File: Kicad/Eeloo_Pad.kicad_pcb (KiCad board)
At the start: 2 copper layers, 61 parts, among them IC1 W25Q16JVUXIQ_TR, IC2 W25Q16JVUXIQ_TR, J1 USB_C_Receptacle_USB2.0_16P, J2 Conn_01x13, J3 SC0914_13_, J4 SC0914_13_, SW1 SW_Push, SW2 SW_Push, SW3 SW_Push, SW4 SW_Push, U1 HT16K33A-28SSOP, U2 HT16K33A-28SSOP, U3 HT16K33A-28SSOP, U4 HT16K33A-28SSOP, U5 HT16K33A-28SSOP, U6 HT16K33A-28SSOP, Y1 ABM8-272-T3, Y2 ABM8-272-T3

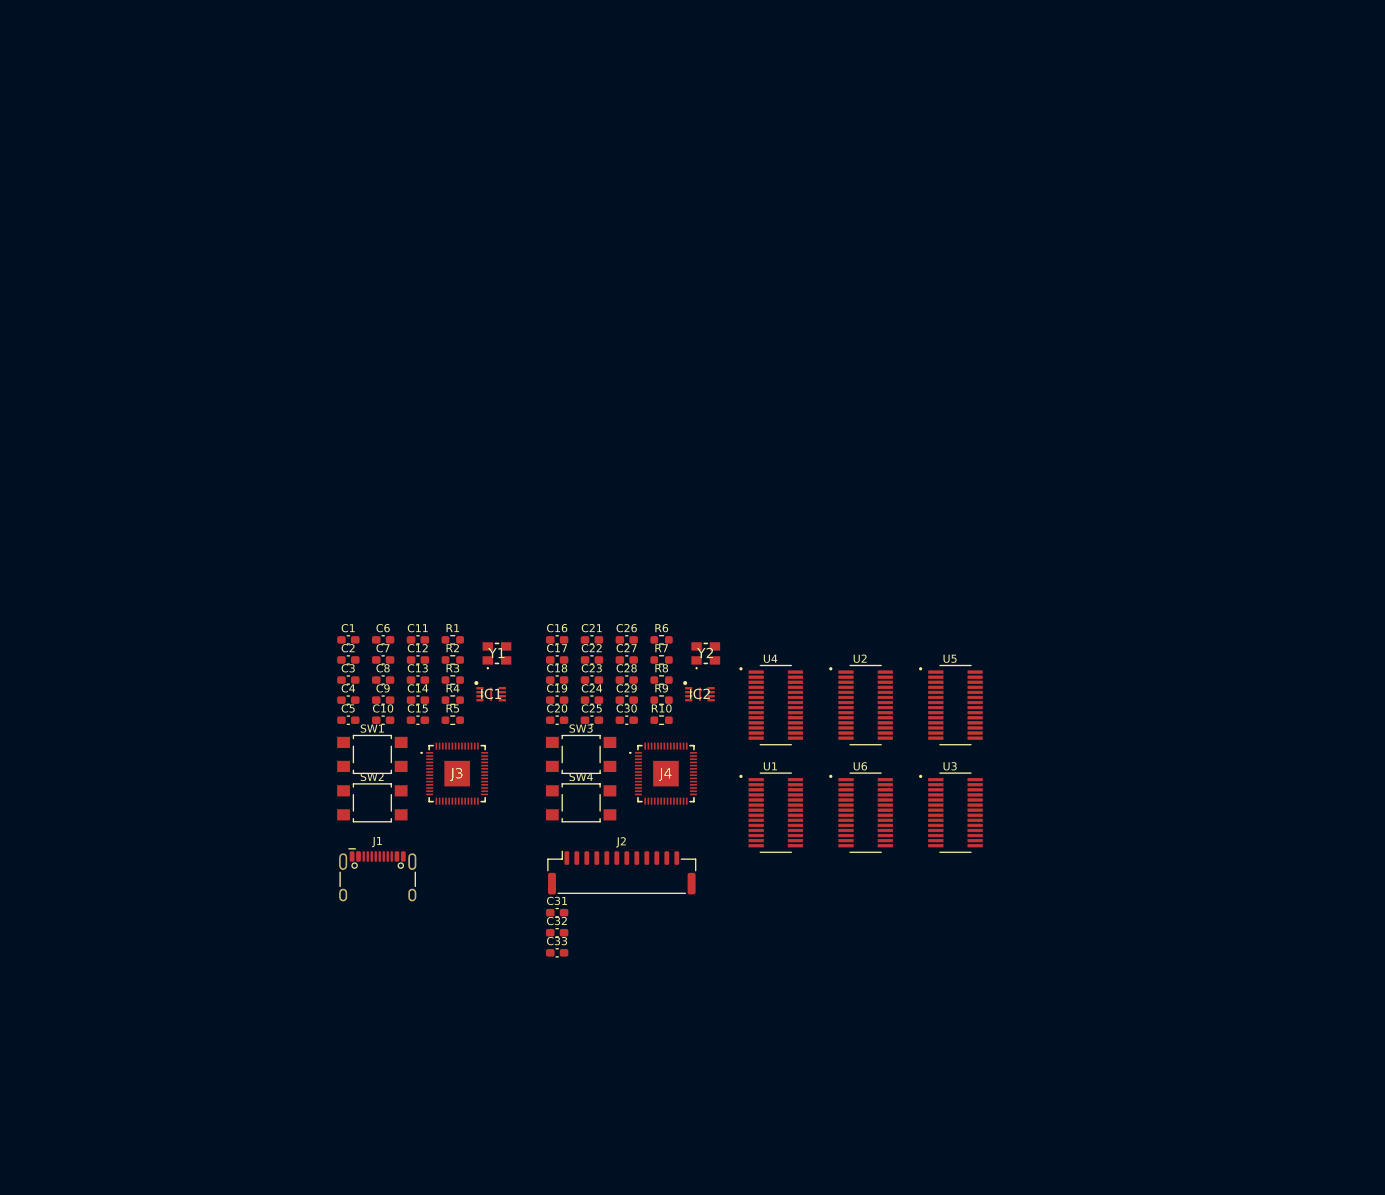
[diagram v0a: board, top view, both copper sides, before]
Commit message: adding multiple component (14 semgent and led)
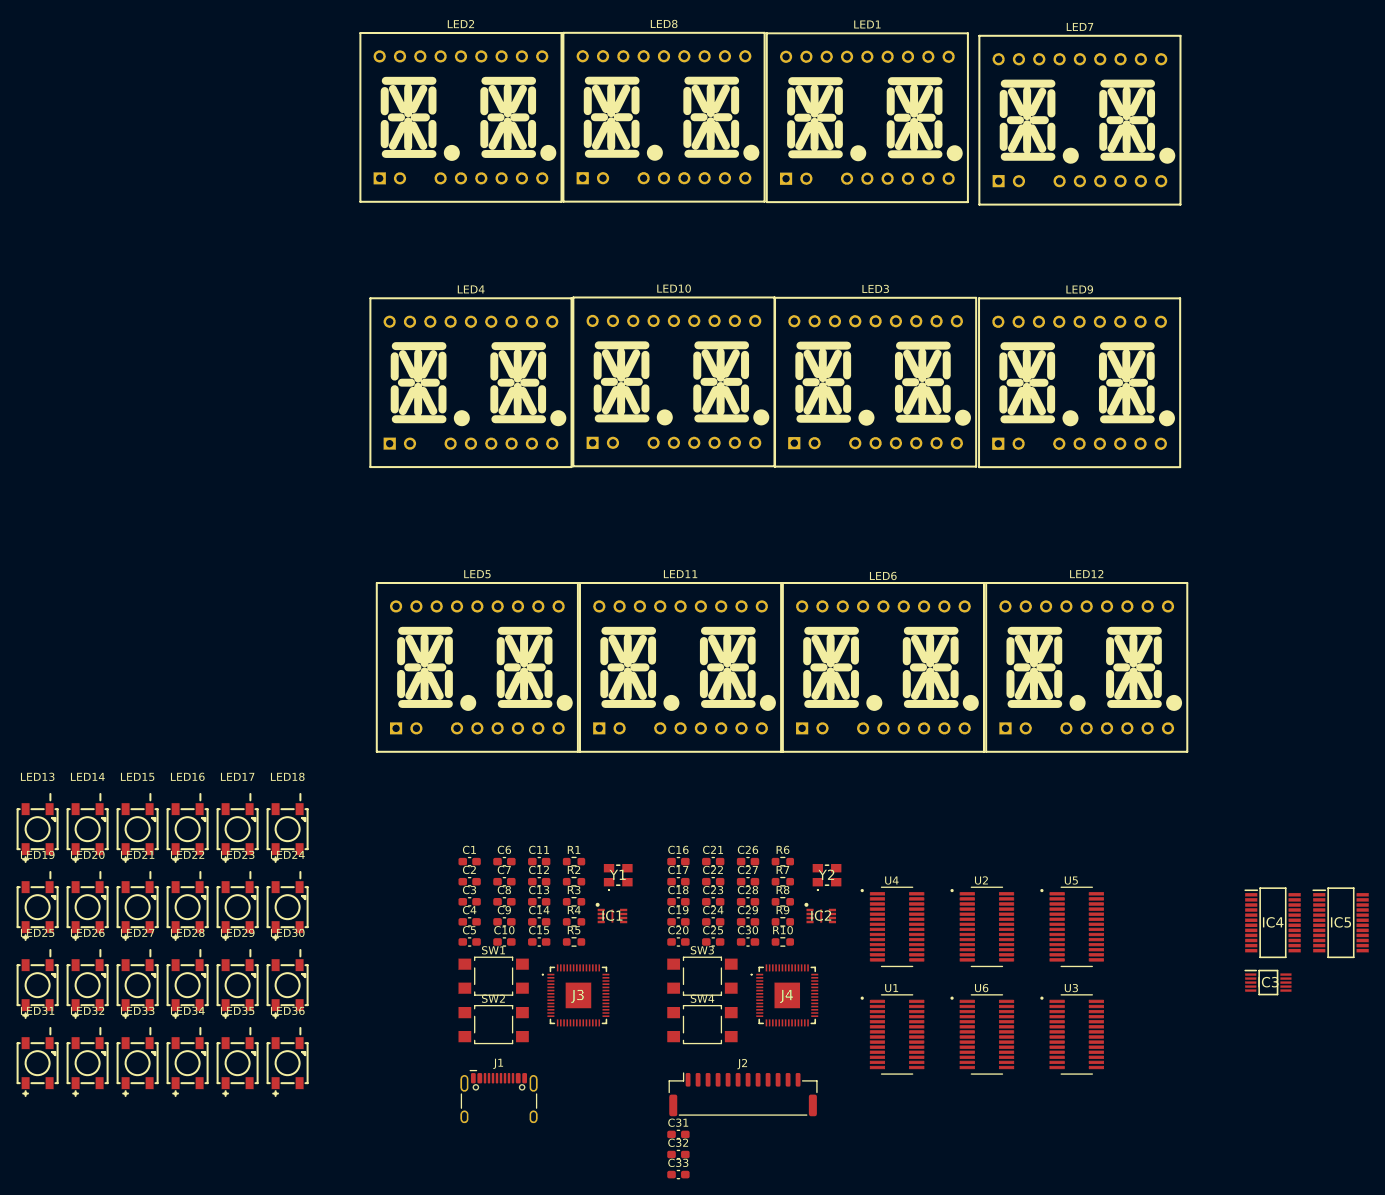
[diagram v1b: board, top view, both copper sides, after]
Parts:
- added IC3: ADS1015IDGST, Eeloo_Pad:SOP50P490X110-10N, F.Cu at (237.6, 138.8)
- added IC4: PCF8575DBQR, Eeloo_Pad:SOP64P600X175-24N, F.Cu at (238.2, 131.3)
- added IC5: PCF8575DBQR, Eeloo_Pad:SOP64P600X175-24N, F.Cu at (246.7, 131.3)
- added LED1: FJ5241AH, Eeloo_Pad:LED-SEG-TH_18P-L25.2-W21.1-P2.54-LS15.2-BL, F.Cu at (187.5, 30.7)
- added LED10: FJ5241AH, Eeloo_Pad:LED-SEG-TH_18P-L25.2-W21.1-P2.54-LS15.2-BL, F.Cu at (163.3, 63.7)
- added LED11: FJ5241AH, Eeloo_Pad:LED-SEG-TH_18P-L25.2-W21.1-P2.54-LS15.2-BL, F.Cu at (164.2, 99.4)
- added LED12: FJ5241AH, Eeloo_Pad:LED-SEG-TH_18P-L25.2-W21.1-P2.54-LS15.2-BL, F.Cu at (214.9, 99.4)
- added LED13: XL-5050RGBC-WS2812B, Eeloo_Pad:LED-SMD_4P-L5.0-W5.0-BL_XL-5050RGBC, F.Cu at (83.8, 119.6)
- added LED14: XL-5050RGBC-WS2812B, Eeloo_Pad:LED-SMD_4P-L5.0-W5.0-BL_XL-5050RGBC, F.Cu at (90.0, 119.6)
- added LED15: XL-5050RGBC-WS2812B, Eeloo_Pad:LED-SMD_4P-L5.0-W5.0-BL_XL-5050RGBC, F.Cu at (96.3, 119.6)
- added LED16: XL-5050RGBC-WS2812B, Eeloo_Pad:LED-SMD_4P-L5.0-W5.0-BL_XL-5050RGBC, F.Cu at (102.5, 119.6)
- added LED17: XL-5050RGBC-WS2812B, Eeloo_Pad:LED-SMD_4P-L5.0-W5.0-BL_XL-5050RGBC, F.Cu at (108.8, 119.6)
- added LED18: XL-5050RGBC-WS2812B, Eeloo_Pad:LED-SMD_4P-L5.0-W5.0-BL_XL-5050RGBC, F.Cu at (115.0, 119.6)
- added LED19: XL-5050RGBC-WS2812B, Eeloo_Pad:LED-SMD_4P-L5.0-W5.0-BL_XL-5050RGBC, F.Cu at (83.8, 129.4)
- added LED2: FJ5241AH, Eeloo_Pad:LED-SEG-TH_18P-L25.2-W21.1-P2.54-LS15.2-BL, F.Cu at (136.7, 30.7)
- added LED20: XL-5050RGBC-WS2812B, Eeloo_Pad:LED-SMD_4P-L5.0-W5.0-BL_XL-5050RGBC, F.Cu at (90.0, 129.4)
- added LED21: XL-5050RGBC-WS2812B, Eeloo_Pad:LED-SMD_4P-L5.0-W5.0-BL_XL-5050RGBC, F.Cu at (96.3, 129.4)
- added LED22: XL-5050RGBC-WS2812B, Eeloo_Pad:LED-SMD_4P-L5.0-W5.0-BL_XL-5050RGBC, F.Cu at (102.5, 129.4)
- added LED23: XL-5050RGBC-WS2812B, Eeloo_Pad:LED-SMD_4P-L5.0-W5.0-BL_XL-5050RGBC, F.Cu at (108.8, 129.4)
- added LED24: XL-5050RGBC-WS2812B, Eeloo_Pad:LED-SMD_4P-L5.0-W5.0-BL_XL-5050RGBC, F.Cu at (115.0, 129.4)
- added LED25: XL-5050RGBC-WS2812B, Eeloo_Pad:LED-SMD_4P-L5.0-W5.0-BL_XL-5050RGBC, F.Cu at (83.8, 139.1)
- added LED26: XL-5050RGBC-WS2812B, Eeloo_Pad:LED-SMD_4P-L5.0-W5.0-BL_XL-5050RGBC, F.Cu at (90.0, 139.1)
- added LED27: XL-5050RGBC-WS2812B, Eeloo_Pad:LED-SMD_4P-L5.0-W5.0-BL_XL-5050RGBC, F.Cu at (96.3, 139.1)
- added LED28: XL-5050RGBC-WS2812B, Eeloo_Pad:LED-SMD_4P-L5.0-W5.0-BL_XL-5050RGBC, F.Cu at (102.5, 139.1)
- added LED29: XL-5050RGBC-WS2812B, Eeloo_Pad:LED-SMD_4P-L5.0-W5.0-BL_XL-5050RGBC, F.Cu at (108.8, 139.1)
- added LED3: FJ5241AH, Eeloo_Pad:LED-SEG-TH_18P-L25.2-W21.1-P2.54-LS15.2-BL, F.Cu at (188.6, 63.8)
- added LED30: XL-5050RGBC-WS2812B, Eeloo_Pad:LED-SMD_4P-L5.0-W5.0-BL_XL-5050RGBC, F.Cu at (115.0, 139.1)
- added LED31: XL-5050RGBC-WS2812B, Eeloo_Pad:LED-SMD_4P-L5.0-W5.0-BL_XL-5050RGBC, F.Cu at (83.8, 148.9)
- added LED32: XL-5050RGBC-WS2812B, Eeloo_Pad:LED-SMD_4P-L5.0-W5.0-BL_XL-5050RGBC, F.Cu at (90.0, 148.9)
- added LED33: XL-5050RGBC-WS2812B, Eeloo_Pad:LED-SMD_4P-L5.0-W5.0-BL_XL-5050RGBC, F.Cu at (96.3, 148.9)
- added LED34: XL-5050RGBC-WS2812B, Eeloo_Pad:LED-SMD_4P-L5.0-W5.0-BL_XL-5050RGBC, F.Cu at (102.5, 148.9)
- added LED35: XL-5050RGBC-WS2812B, Eeloo_Pad:LED-SMD_4P-L5.0-W5.0-BL_XL-5050RGBC, F.Cu at (108.8, 148.9)
- added LED36: XL-5050RGBC-WS2812B, Eeloo_Pad:LED-SMD_4P-L5.0-W5.0-BL_XL-5050RGBC, F.Cu at (115.0, 148.9)
- added LED4: FJ5241AH, Eeloo_Pad:LED-SEG-TH_18P-L25.2-W21.1-P2.54-LS15.2-BL, F.Cu at (138.0, 63.8)
- added LED5: FJ5241AH, Eeloo_Pad:LED-SEG-TH_18P-L25.2-W21.1-P2.54-LS15.2-BL, F.Cu at (138.8, 99.4)
- added LED6: FJ5241AH, Eeloo_Pad:LED-SEG-TH_18P-L25.2-W21.1-P2.54-LS15.2-BL, F.Cu at (189.5, 99.4)
- added LED7: FJ5241AH, Eeloo_Pad:LED-SEG-TH_18P-L25.2-W21.1-P2.54-LS15.2-BL, F.Cu at (214.1, 31.0)
- added LED8: FJ5241AH, Eeloo_Pad:LED-SEG-TH_18P-L25.2-W21.1-P2.54-LS15.2-BL, F.Cu at (162.1, 30.6)
- added LED9: FJ5241AH, Eeloo_Pad:LED-SEG-TH_18P-L25.2-W21.1-P2.54-LS15.2-BL, F.Cu at (214.1, 63.8)
- moved R10 31.6 mm to (177.0, 133.7)
- moved U1 31.6 mm to (191.2, 145.3)
- moved C5 31.6 mm to (137.8, 133.7)
- moved SW1 31.6 mm to (140.8, 138.0)
- moved J2 31.6 mm to (172.0, 152.8)
- moved R6 31.6 mm to (177.0, 123.7)
- moved R7 31.6 mm to (177.0, 126.2)
- moved R8 31.6 mm to (177.0, 128.7)
- moved U4 31.6 mm to (191.2, 131.9)
- moved C10 31.6 mm to (142.2, 133.7)
- moved C15 31.6 mm to (146.5, 133.7)
- moved C20 31.6 mm to (163.9, 133.7)
- moved C25 31.6 mm to (168.3, 133.7)
- moved C30 31.6 mm to (172.6, 133.7)
- moved J1 31.6 mm to (141.5, 154.5)
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
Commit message: working on the 14 segment schematics
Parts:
- moved U1 138.5 mm to (116.0, 29.0)
- moved U2 106.3 mm to (233.0, 30.0)
- moved U5 99.4 mm to (120.0, 98.6)
- moved U4 99.4 mm to (119.0, 63.5)
- moved U3 83.6 mm to (233.0, 64.0)
- moved U6 55.3 mm to (233.0, 99.1)
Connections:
- LED1 pad 1: unconnected-(LED1-E-Pad1) -> /control_module/seg_4x14_module1/E
- LED1 pad 10: unconnected-(LED1-B-Pad10) -> /control_module/seg_4x14_module1/A1
- LED1 pad 11: unconnected-(LED1-DIG2-Pad11) -> /control_module/seg_4x14_module1/COM1
- LED1 pad 12: unconnected-(LED1-A-Pad12) -> /control_module/seg_4x14_module1/A
- LED1 pad 13: unconnected-(LED1-G1-Pad13) -> /control_module/seg_4x14_module1/G1
- LED1 pad 14: unconnected-(LED1-K-Pad14) -> /control_module/seg_4x14_module1/K
- LED1 pad 15: unconnected-(LED1-J-Pad15) -> /control_module/seg_4x14_module1/J
- LED1 pad 16: unconnected-(LED1-DIG1-Pad16) -> /control_module/seg_4x14_module1/AD
- LED1 pad 17: unconnected-(LED1-H-Pad17) -> /control_module/seg_4x14_module1/H
- LED1 pad 18: unconnected-(LED1-F-Pad18) -> /control_module/seg_4x14_module1/F
- LED1 pad 2: unconnected-(LED1-N-Pad2) -> /control_module/seg_4x14_module1/N
- LED1 pad 4: unconnected-(LED1-M-Pad4) -> /control_module/seg_4x14_module1/M
- LED1 pad 5: unconnected-(LED1-L-Pad5) -> /control_module/seg_4x14_module1/L
- LED1 pad 6: unconnected-(LED1-G2-Pad6) -> /control_module/seg_4x14_module1/G2
- LED1 pad 7: unconnected-(LED1-D-Pad7) -> /control_module/seg_4x14_module1/D
- LED1 pad 8: unconnected-(LED1-DP-Pad8) -> /control_module/seg_4x14_module1/DP
- LED1 pad 9: unconnected-(LED1-C-Pad9) -> /control_module/seg_4x14_module1/A0
- LED10 pad 1: unconnected-(LED10-E-Pad1) -> /control_module/seg_4x14_module3/E
- LED10 pad 10: unconnected-(LED10-B-Pad10) -> /control_module/seg_4x14_module3/A1
- LED10 pad 11: unconnected-(LED10-DIG2-Pad11) -> /control_module/seg_4x14_module3/COM3
- LED10 pad 12: unconnected-(LED10-A-Pad12) -> /control_module/seg_4x14_module3/A
- LED10 pad 13: unconnected-(LED10-G1-Pad13) -> /control_module/seg_4x14_module3/G1
- LED10 pad 14: unconnected-(LED10-K-Pad14) -> /control_module/seg_4x14_module3/K
- LED10 pad 15: unconnected-(LED10-J-Pad15) -> /control_module/seg_4x14_module3/J
- LED10 pad 16: unconnected-(LED10-DIG1-Pad16) -> /control_module/seg_4x14_module3/COM2
- LED10 pad 17: unconnected-(LED10-H-Pad17) -> /control_module/seg_4x14_module3/H
- LED10 pad 18: unconnected-(LED10-F-Pad18) -> /control_module/seg_4x14_module3/F
- LED10 pad 2: unconnected-(LED10-N-Pad2) -> /control_module/seg_4x14_module3/N
- LED10 pad 4: unconnected-(LED10-M-Pad4) -> /control_module/seg_4x14_module3/M
- LED10 pad 5: unconnected-(LED10-L-Pad5) -> /control_module/seg_4x14_module3/L
- LED10 pad 6: unconnected-(LED10-G2-Pad6) -> /control_module/seg_4x14_module3/G2
- LED10 pad 7: unconnected-(LED10-D-Pad7) -> /control_module/seg_4x14_module3/D
- LED10 pad 8: unconnected-(LED10-DP-Pad8) -> /control_module/seg_4x14_module3/DP
- LED10 pad 9: unconnected-(LED10-C-Pad9) -> /control_module/seg_4x14_module3/A0
- LED11 pad 1: unconnected-(LED11-E-Pad1) -> /control_module/seg_4x14_module4/E
- LED11 pad 10: unconnected-(LED11-B-Pad10) -> /control_module/seg_4x14_module4/A1
- LED11 pad 11: unconnected-(LED11-DIG2-Pad11) -> /control_module/seg_4x14_module4/COM3
- LED11 pad 12: unconnected-(LED11-A-Pad12) -> /control_module/seg_4x14_module4/A
- LED11 pad 13: unconnected-(LED11-G1-Pad13) -> /control_module/seg_4x14_module4/G1
- LED11 pad 14: unconnected-(LED11-K-Pad14) -> /control_module/seg_4x14_module4/K
- LED11 pad 15: unconnected-(LED11-J-Pad15) -> /control_module/seg_4x14_module4/J
- LED11 pad 16: unconnected-(LED11-DIG1-Pad16) -> /control_module/seg_4x14_module4/COM2
- LED11 pad 17: unconnected-(LED11-H-Pad17) -> /control_module/seg_4x14_module4/H
- LED11 pad 18: unconnected-(LED11-F-Pad18) -> /control_module/seg_4x14_module4/F
- LED11 pad 2: unconnected-(LED11-N-Pad2) -> /control_module/seg_4x14_module4/N
- LED11 pad 4: unconnected-(LED11-M-Pad4) -> /control_module/seg_4x14_module4/M
- LED11 pad 5: unconnected-(LED11-L-Pad5) -> /control_module/seg_4x14_module4/L
- LED11 pad 6: unconnected-(LED11-G2-Pad6) -> /control_module/seg_4x14_module4/G2
- LED11 pad 7: unconnected-(LED11-D-Pad7) -> /control_module/seg_4x14_module4/D
- LED11 pad 8: unconnected-(LED11-DP-Pad8) -> /control_module/seg_4x14_module4/DP
- LED11 pad 9: unconnected-(LED11-C-Pad9) -> /control_module/seg_4x14_module4/A0
- LED12 pad 1: unconnected-(LED12-E-Pad1) -> /control_module/seg_4x14_module5/E
- LED12 pad 10: unconnected-(LED12-B-Pad10) -> /control_module/seg_4x14_module5/A1
- LED12 pad 11: unconnected-(LED12-DIG2-Pad11) -> /control_module/seg_4x14_module5/COM3
- LED12 pad 12: unconnected-(LED12-A-Pad12) -> /control_module/seg_4x14_module5/A
- LED12 pad 13: unconnected-(LED12-G1-Pad13) -> /control_module/seg_4x14_module5/G1
- LED12 pad 14: unconnected-(LED12-K-Pad14) -> /control_module/seg_4x14_module5/K
- LED12 pad 15: unconnected-(LED12-J-Pad15) -> /control_module/seg_4x14_module5/J
- LED12 pad 16: unconnected-(LED12-DIG1-Pad16) -> /control_module/seg_4x14_module5/COM2
- LED12 pad 17: unconnected-(LED12-H-Pad17) -> /control_module/seg_4x14_module5/H
- LED12 pad 18: unconnected-(LED12-F-Pad18) -> /control_module/seg_4x14_module5/F
- LED12 pad 2: unconnected-(LED12-N-Pad2) -> /control_module/seg_4x14_module5/N
- LED12 pad 4: unconnected-(LED12-M-Pad4) -> /control_module/seg_4x14_module5/M
- LED12 pad 5: unconnected-(LED12-L-Pad5) -> /control_module/seg_4x14_module5/L
- LED12 pad 6: unconnected-(LED12-G2-Pad6) -> /control_module/seg_4x14_module5/G2
- LED12 pad 7: unconnected-(LED12-D-Pad7) -> /control_module/seg_4x14_module5/D
- LED12 pad 8: unconnected-(LED12-DP-Pad8) -> /control_module/seg_4x14_module5/DP
- LED12 pad 9: unconnected-(LED12-C-Pad9) -> /control_module/seg_4x14_module5/A0
- LED2 pad 1: unconnected-(LED2-E-Pad1) -> /control_module/seg_4x14_module/E
- LED2 pad 10: unconnected-(LED2-B-Pad10) -> /control_module/seg_4x14_module/A1
- LED2 pad 11: unconnected-(LED2-DIG2-Pad11) -> /control_module/seg_4x14_module/COM1
- LED2 pad 12: unconnected-(LED2-A-Pad12) -> /control_module/seg_4x14_module/A
- LED2 pad 13: unconnected-(LED2-G1-Pad13) -> /control_module/seg_4x14_module/G1
- LED2 pad 14: unconnected-(LED2-K-Pad14) -> /control_module/seg_4x14_module/K
- LED2 pad 15: unconnected-(LED2-J-Pad15) -> /control_module/seg_4x14_module/J
- LED2 pad 16: unconnected-(LED2-DIG1-Pad16) -> /control_module/seg_4x14_module/AD
- LED2 pad 17: unconnected-(LED2-H-Pad17) -> /control_module/seg_4x14_module/H
- LED2 pad 18: unconnected-(LED2-F-Pad18) -> /control_module/seg_4x14_module/F
- LED2 pad 2: unconnected-(LED2-N-Pad2) -> /control_module/seg_4x14_module/N
- LED2 pad 4: unconnected-(LED2-M-Pad4) -> /control_module/seg_4x14_module/M
- LED2 pad 5: unconnected-(LED2-L-Pad5) -> /control_module/seg_4x14_module/L
- LED2 pad 6: unconnected-(LED2-G2-Pad6) -> /control_module/seg_4x14_module/G2
- LED2 pad 7: unconnected-(LED2-D-Pad7) -> /control_module/seg_4x14_module/D
- LED2 pad 8: unconnected-(LED2-DP-Pad8) -> /control_module/seg_4x14_module/DP
- LED2 pad 9: unconnected-(LED2-C-Pad9) -> /control_module/seg_4x14_module/A0
- LED3 pad 1: unconnected-(LED3-E-Pad1) -> /control_module/seg_4x14_module2/E
- LED3 pad 10: unconnected-(LED3-B-Pad10) -> /control_module/seg_4x14_module2/A1
- LED3 pad 11: unconnected-(LED3-DIG2-Pad11) -> /control_module/seg_4x14_module2/COM1
- LED3 pad 12: unconnected-(LED3-A-Pad12) -> /control_module/seg_4x14_module2/A
- LED3 pad 13: unconnected-(LED3-G1-Pad13) -> /control_module/seg_4x14_module2/G1
- LED3 pad 14: unconnected-(LED3-K-Pad14) -> /control_module/seg_4x14_module2/K
- LED3 pad 15: unconnected-(LED3-J-Pad15) -> /control_module/seg_4x14_module2/J
- LED3 pad 16: unconnected-(LED3-DIG1-Pad16) -> /control_module/seg_4x14_module2/AD
- LED3 pad 17: unconnected-(LED3-H-Pad17) -> /control_module/seg_4x14_module2/H
- LED3 pad 18: unconnected-(LED3-F-Pad18) -> /control_module/seg_4x14_module2/F
- LED3 pad 2: unconnected-(LED3-N-Pad2) -> /control_module/seg_4x14_module2/N
- LED3 pad 4: unconnected-(LED3-M-Pad4) -> /control_module/seg_4x14_module2/M
- LED3 pad 5: unconnected-(LED3-L-Pad5) -> /control_module/seg_4x14_module2/L
- LED3 pad 6: unconnected-(LED3-G2-Pad6) -> /control_module/seg_4x14_module2/G2
- LED3 pad 7: unconnected-(LED3-D-Pad7) -> /control_module/seg_4x14_module2/D
- LED3 pad 8: unconnected-(LED3-DP-Pad8) -> /control_module/seg_4x14_module2/DP
- LED3 pad 9: unconnected-(LED3-C-Pad9) -> /control_module/seg_4x14_module2/A0
- LED4 pad 1: unconnected-(LED4-E-Pad1) -> /control_module/seg_4x14_module3/E
- LED4 pad 10: unconnected-(LED4-B-Pad10) -> /control_module/seg_4x14_module3/A1
- LED4 pad 11: unconnected-(LED4-DIG2-Pad11) -> /control_module/seg_4x14_module3/COM1
- LED4 pad 12: unconnected-(LED4-A-Pad12) -> /control_module/seg_4x14_module3/A
- LED4 pad 13: unconnected-(LED4-G1-Pad13) -> /control_module/seg_4x14_module3/G1
- LED4 pad 14: unconnected-(LED4-K-Pad14) -> /control_module/seg_4x14_module3/K
- LED4 pad 15: unconnected-(LED4-J-Pad15) -> /control_module/seg_4x14_module3/J
- LED4 pad 16: unconnected-(LED4-DIG1-Pad16) -> /control_module/seg_4x14_module3/AD
- LED4 pad 17: unconnected-(LED4-H-Pad17) -> /control_module/seg_4x14_module3/H
- LED4 pad 18: unconnected-(LED4-F-Pad18) -> /control_module/seg_4x14_module3/F
- LED4 pad 2: unconnected-(LED4-N-Pad2) -> /control_module/seg_4x14_module3/N
- LED4 pad 4: unconnected-(LED4-M-Pad4) -> /control_module/seg_4x14_module3/M
- LED4 pad 5: unconnected-(LED4-L-Pad5) -> /control_module/seg_4x14_module3/L
- LED4 pad 6: unconnected-(LED4-G2-Pad6) -> /control_module/seg_4x14_module3/G2
- LED4 pad 7: unconnected-(LED4-D-Pad7) -> /control_module/seg_4x14_module3/D
- LED4 pad 8: unconnected-(LED4-DP-Pad8) -> /control_module/seg_4x14_module3/DP
- LED4 pad 9: unconnected-(LED4-C-Pad9) -> /control_module/seg_4x14_module3/A0
- LED5 pad 1: unconnected-(LED5-E-Pad1) -> /control_module/seg_4x14_module4/E
- LED5 pad 10: unconnected-(LED5-B-Pad10) -> /control_module/seg_4x14_module4/A1
- LED5 pad 11: unconnected-(LED5-DIG2-Pad11) -> /control_module/seg_4x14_module4/COM1
- LED5 pad 12: unconnected-(LED5-A-Pad12) -> /control_module/seg_4x14_module4/A
- LED5 pad 13: unconnected-(LED5-G1-Pad13) -> /control_module/seg_4x14_module4/G1
- LED5 pad 14: unconnected-(LED5-K-Pad14) -> /control_module/seg_4x14_module4/K
- LED5 pad 15: unconnected-(LED5-J-Pad15) -> /control_module/seg_4x14_module4/J
- LED5 pad 16: unconnected-(LED5-DIG1-Pad16) -> /control_module/seg_4x14_module4/AD
- LED5 pad 17: unconnected-(LED5-H-Pad17) -> /control_module/seg_4x14_module4/H
- LED5 pad 18: unconnected-(LED5-F-Pad18) -> /control_module/seg_4x14_module4/F
- LED5 pad 2: unconnected-(LED5-N-Pad2) -> /control_module/seg_4x14_module4/N
- LED5 pad 4: unconnected-(LED5-M-Pad4) -> /control_module/seg_4x14_module4/M
- LED5 pad 5: unconnected-(LED5-L-Pad5) -> /control_module/seg_4x14_module4/L
- LED5 pad 6: unconnected-(LED5-G2-Pad6) -> /control_module/seg_4x14_module4/G2
- LED5 pad 7: unconnected-(LED5-D-Pad7) -> /control_module/seg_4x14_module4/D
- LED5 pad 8: unconnected-(LED5-DP-Pad8) -> /control_module/seg_4x14_module4/DP
- LED5 pad 9: unconnected-(LED5-C-Pad9) -> /control_module/seg_4x14_module4/A0
- LED6 pad 1: unconnected-(LED6-E-Pad1) -> /control_module/seg_4x14_module5/E
- LED6 pad 10: unconnected-(LED6-B-Pad10) -> /control_module/seg_4x14_module5/A1
- LED6 pad 11: unconnected-(LED6-DIG2-Pad11) -> /control_module/seg_4x14_module5/COM1
- LED6 pad 12: unconnected-(LED6-A-Pad12) -> /control_module/seg_4x14_module5/A
- LED6 pad 13: unconnected-(LED6-G1-Pad13) -> /control_module/seg_4x14_module5/G1
- LED6 pad 14: unconnected-(LED6-K-Pad14) -> /control_module/seg_4x14_module5/K
- LED6 pad 15: unconnected-(LED6-J-Pad15) -> /control_module/seg_4x14_module5/J
- LED6 pad 16: unconnected-(LED6-DIG1-Pad16) -> /control_module/seg_4x14_module5/AD
- LED6 pad 17: unconnected-(LED6-H-Pad17) -> /control_module/seg_4x14_module5/H
- LED6 pad 18: unconnected-(LED6-F-Pad18) -> /control_module/seg_4x14_module5/F
- LED6 pad 2: unconnected-(LED6-N-Pad2) -> /control_module/seg_4x14_module5/N
- LED6 pad 4: unconnected-(LED6-M-Pad4) -> /control_module/seg_4x14_module5/M
- LED6 pad 5: unconnected-(LED6-L-Pad5) -> /control_module/seg_4x14_module5/L
- LED6 pad 6: unconnected-(LED6-G2-Pad6) -> /control_module/seg_4x14_module5/G2
- LED6 pad 7: unconnected-(LED6-D-Pad7) -> /control_module/seg_4x14_module5/D
- LED6 pad 8: unconnected-(LED6-DP-Pad8) -> /control_module/seg_4x14_module5/DP
- LED6 pad 9: unconnected-(LED6-C-Pad9) -> /control_module/seg_4x14_module5/A0
- LED7 pad 1: unconnected-(LED7-E-Pad1) -> /control_module/seg_4x14_module1/E
- LED7 pad 10: unconnected-(LED7-B-Pad10) -> /control_module/seg_4x14_module1/A1
- LED7 pad 11: unconnected-(LED7-DIG2-Pad11) -> /control_module/seg_4x14_module1/COM3
- LED7 pad 12: unconnected-(LED7-A-Pad12) -> /control_module/seg_4x14_module1/A
- LED7 pad 13: unconnected-(LED7-G1-Pad13) -> /control_module/seg_4x14_module1/G1
- LED7 pad 14: unconnected-(LED7-K-Pad14) -> /control_module/seg_4x14_module1/K
- LED7 pad 15: unconnected-(LED7-J-Pad15) -> /control_module/seg_4x14_module1/J
- LED7 pad 16: unconnected-(LED7-DIG1-Pad16) -> /control_module/seg_4x14_module1/COM2
- LED7 pad 17: unconnected-(LED7-H-Pad17) -> /control_module/seg_4x14_module1/H
- LED7 pad 18: unconnected-(LED7-F-Pad18) -> /control_module/seg_4x14_module1/F
- LED7 pad 2: unconnected-(LED7-N-Pad2) -> /control_module/seg_4x14_module1/N
- LED7 pad 4: unconnected-(LED7-M-Pad4) -> /control_module/seg_4x14_module1/M
- LED7 pad 5: unconnected-(LED7-L-Pad5) -> /control_module/seg_4x14_module1/L
- LED7 pad 6: unconnected-(LED7-G2-Pad6) -> /control_module/seg_4x14_module1/G2
- LED7 pad 7: unconnected-(LED7-D-Pad7) -> /control_module/seg_4x14_module1/D
- LED7 pad 8: unconnected-(LED7-DP-Pad8) -> /control_module/seg_4x14_module1/DP
- LED7 pad 9: unconnected-(LED7-C-Pad9) -> /control_module/seg_4x14_module1/A0
- LED8 pad 1: unconnected-(LED8-E-Pad1) -> /control_module/seg_4x14_module/E
- LED8 pad 10: unconnected-(LED8-B-Pad10) -> /control_module/seg_4x14_module/A1
- LED8 pad 11: unconnected-(LED8-DIG2-Pad11) -> /control_module/seg_4x14_module/COM3
- LED8 pad 12: unconnected-(LED8-A-Pad12) -> /control_module/seg_4x14_module/A
- LED8 pad 13: unconnected-(LED8-G1-Pad13) -> /control_module/seg_4x14_module/G1
- LED8 pad 14: unconnected-(LED8-K-Pad14) -> /control_module/seg_4x14_module/K
- LED8 pad 15: unconnected-(LED8-J-Pad15) -> /control_module/seg_4x14_module/J
- LED8 pad 16: unconnected-(LED8-DIG1-Pad16) -> /control_module/seg_4x14_module/COM2
- LED8 pad 17: unconnected-(LED8-H-Pad17) -> /control_module/seg_4x14_module/H
- LED8 pad 18: unconnected-(LED8-F-Pad18) -> /control_module/seg_4x14_module/F
- LED8 pad 2: unconnected-(LED8-N-Pad2) -> /control_module/seg_4x14_module/N
- LED8 pad 4: unconnected-(LED8-M-Pad4) -> /control_module/seg_4x14_module/M
- LED8 pad 5: unconnected-(LED8-L-Pad5) -> /control_module/seg_4x14_module/L
- LED8 pad 6: unconnected-(LED8-G2-Pad6) -> /control_module/seg_4x14_module/G2
- LED8 pad 7: unconnected-(LED8-D-Pad7) -> /control_module/seg_4x14_module/D
- LED8 pad 8: unconnected-(LED8-DP-Pad8) -> /control_module/seg_4x14_module/DP
- LED8 pad 9: unconnected-(LED8-C-Pad9) -> /control_module/seg_4x14_module/A0
- LED9 pad 1: unconnected-(LED9-E-Pad1) -> /control_module/seg_4x14_module2/E
- LED9 pad 10: unconnected-(LED9-B-Pad10) -> /control_module/seg_4x14_module2/A1
- LED9 pad 11: unconnected-(LED9-DIG2-Pad11) -> /control_module/seg_4x14_module2/COM3
- LED9 pad 12: unconnected-(LED9-A-Pad12) -> /control_module/seg_4x14_module2/A
- LED9 pad 13: unconnected-(LED9-G1-Pad13) -> /control_module/seg_4x14_module2/G1
- LED9 pad 14: unconnected-(LED9-K-Pad14) -> /control_module/seg_4x14_module2/K
- LED9 pad 15: unconnected-(LED9-J-Pad15) -> /control_module/seg_4x14_module2/J
- LED9 pad 16: unconnected-(LED9-DIG1-Pad16) -> /control_module/seg_4x14_module2/COM2
- LED9 pad 17: unconnected-(LED9-H-Pad17) -> /control_module/seg_4x14_module2/H
- LED9 pad 18: unconnected-(LED9-F-Pad18) -> /control_module/seg_4x14_module2/F
- LED9 pad 2: unconnected-(LED9-N-Pad2) -> /control_module/seg_4x14_module2/N
- LED9 pad 4: unconnected-(LED9-M-Pad4) -> /control_module/seg_4x14_module2/M
- LED9 pad 5: unconnected-(LED9-L-Pad5) -> /control_module/seg_4x14_module2/L
- LED9 pad 6: unconnected-(LED9-G2-Pad6) -> /control_module/seg_4x14_module2/G2
- LED9 pad 7: unconnected-(LED9-D-Pad7) -> /control_module/seg_4x14_module2/D
- LED9 pad 8: unconnected-(LED9-DP-Pad8) -> /control_module/seg_4x14_module2/DP
- LED9 pad 9: unconnected-(LED9-C-Pad9) -> /control_module/seg_4x14_module2/A0
- U1 pad 11: unconnected-(U1-ROW14/K12-Pad11) -> /control_module/seg_4x14_module/DP
- U1 pad 12: unconnected-(U1-ROW13/K11-Pad12) -> /control_module/seg_4x14_module/N
- U1 pad 13: unconnected-(U1-ROW12/K10-Pad13) -> /control_module/seg_4x14_module/M
- U1 pad 14: unconnected-(U1-ROW11/K9-Pad14) -> /control_module/seg_4x14_module/L
- U1 pad 15: unconnected-(U1-ROW10/K8-Pad15) -> /control_module/seg_4x14_module/K
- U1 pad 16: unconnected-(U1-ROW9/K7-Pad16) -> /control_module/seg_4x14_module/J
- U1 pad 17: unconnected-(U1-ROW8/K6-Pad17) -> /control_module/seg_4x14_module/H
- U1 pad 18: unconnected-(U1-ROW7/K5-Pad18) -> /control_module/seg_4x14_module/G2
- U1 pad 19: unconnected-(U1-ROW6/K4-Pad19) -> /control_module/seg_4x14_module/G1
- U1 pad 2: unconnected-(U1-COM0/AD-Pad2) -> /control_module/seg_4x14_module/AD
- U1 pad 20: unconnected-(U1-ROW5/K3-Pad20) -> /control_module/seg_4x14_module/F
- U1 pad 21: unconnected-(U1-ROW4/K2-Pad21) -> /control_module/seg_4x14_module/E
- U1 pad 22: unconnected-(U1-ROW3/K1-Pad22) -> /control_module/seg_4x14_module/D
- U1 pad 23: unconnected-(U1-ROW2/A0-Pad23) -> /control_module/seg_4x14_module/A0
- U1 pad 24: unconnected-(U1-ROW1/A1-Pad24) -> /control_module/seg_4x14_module/A1
- U1 pad 25: unconnected-(U1-ROW0/A2-Pad25) -> /control_module/seg_4x14_module/A
- U1 pad 3: unconnected-(U1-COM1/KS0-Pad3) -> /control_module/seg_4x14_module/COM1
- U1 pad 4: unconnected-(U1-COM2/KS1-Pad4) -> /control_module/seg_4x14_module/COM2
- U1 pad 5: unconnected-(U1-COM3/KS2-Pad5) -> /control_module/seg_4x14_module/COM3
- U2 pad 11: unconnected-(U2-ROW14/K12-Pad11) -> /control_module/seg_4x14_module1/DP
- U2 pad 12: unconnected-(U2-ROW13/K11-Pad12) -> /control_module/seg_4x14_module1/N
- U2 pad 13: unconnected-(U2-ROW12/K10-Pad13) -> /control_module/seg_4x14_module1/M
- U2 pad 14: unconnected-(U2-ROW11/K9-Pad14) -> /control_module/seg_4x14_module1/L
- U2 pad 15: unconnected-(U2-ROW10/K8-Pad15) -> /control_module/seg_4x14_module1/K
- U2 pad 16: unconnected-(U2-ROW9/K7-Pad16) -> /control_module/seg_4x14_module1/J
- U2 pad 17: unconnected-(U2-ROW8/K6-Pad17) -> /control_module/seg_4x14_module1/H
- U2 pad 18: unconnected-(U2-ROW7/K5-Pad18) -> /control_module/seg_4x14_module1/G2
- U2 pad 19: unconnected-(U2-ROW6/K4-Pad19) -> /control_module/seg_4x14_module1/G1
- U2 pad 2: unconnected-(U2-COM0/AD-Pad2) -> /control_module/seg_4x14_module1/AD
- U2 pad 20: unconnected-(U2-ROW5/K3-Pad20) -> /control_module/seg_4x14_module1/F
- U2 pad 21: unconnected-(U2-ROW4/K2-Pad21) -> /control_module/seg_4x14_module1/E
- U2 pad 22: unconnected-(U2-ROW3/K1-Pad22) -> /control_module/seg_4x14_module1/D
- U2 pad 23: unconnected-(U2-ROW2/A0-Pad23) -> /control_module/seg_4x14_module1/A0
- U2 pad 24: unconnected-(U2-ROW1/A1-Pad24) -> /control_module/seg_4x14_module1/A1
- U2 pad 25: unconnected-(U2-ROW0/A2-Pad25) -> /control_module/seg_4x14_module1/A
- U2 pad 3: unconnected-(U2-COM1/KS0-Pad3) -> /control_module/seg_4x14_module1/COM1
- U2 pad 4: unconnected-(U2-COM2/KS1-Pad4) -> /control_module/seg_4x14_module1/COM2
- U2 pad 5: unconnected-(U2-COM3/KS2-Pad5) -> /control_module/seg_4x14_module1/COM3
- U3 pad 11: unconnected-(U3-ROW14/K12-Pad11) -> /control_module/seg_4x14_module2/DP
- U3 pad 12: unconnected-(U3-ROW13/K11-Pad12) -> /control_module/seg_4x14_module2/N
- U3 pad 13: unconnected-(U3-ROW12/K10-Pad13) -> /control_module/seg_4x14_module2/M
- U3 pad 14: unconnected-(U3-ROW11/K9-Pad14) -> /control_module/seg_4x14_module2/L
- U3 pad 15: unconnected-(U3-ROW10/K8-Pad15) -> /control_module/seg_4x14_module2/K
- U3 pad 16: unconnected-(U3-ROW9/K7-Pad16) -> /control_module/seg_4x14_module2/J
- U3 pad 17: unconnected-(U3-ROW8/K6-Pad17) -> /control_module/seg_4x14_module2/H
- U3 pad 18: unconnected-(U3-ROW7/K5-Pad18) -> /control_module/seg_4x14_module2/G2
- U3 pad 19: unconnected-(U3-ROW6/K4-Pad19) -> /control_module/seg_4x14_module2/G1
- U3 pad 2: unconnected-(U3-COM0/AD-Pad2) -> /control_module/seg_4x14_module2/AD
- U3 pad 20: unconnected-(U3-ROW5/K3-Pad20) -> /control_module/seg_4x14_module2/F
- U3 pad 21: unconnected-(U3-ROW4/K2-Pad21) -> /control_module/seg_4x14_module2/E
- U3 pad 22: unconnected-(U3-ROW3/K1-Pad22) -> /control_module/seg_4x14_module2/D
- U3 pad 23: unconnected-(U3-ROW2/A0-Pad23) -> /control_module/seg_4x14_module2/A0
- U3 pad 24: unconnected-(U3-ROW1/A1-Pad24) -> /control_module/seg_4x14_module2/A1
- U3 pad 25: unconnected-(U3-ROW0/A2-Pad25) -> /control_module/seg_4x14_module2/A
- U3 pad 3: unconnected-(U3-COM1/KS0-Pad3) -> /control_module/seg_4x14_module2/COM1
- U3 pad 4: unconnected-(U3-COM2/KS1-Pad4) -> /control_module/seg_4x14_module2/COM2
- U3 pad 5: unconnected-(U3-COM3/KS2-Pad5) -> /control_module/seg_4x14_module2/COM3
- U4 pad 11: unconnected-(U4-ROW14/K12-Pad11) -> /control_module/seg_4x14_module3/DP
- U4 pad 12: unconnected-(U4-ROW13/K11-Pad12) -> /control_module/seg_4x14_module3/N
- U4 pad 13: unconnected-(U4-ROW12/K10-Pad13) -> /control_module/seg_4x14_module3/M
- U4 pad 14: unconnected-(U4-ROW11/K9-Pad14) -> /control_module/seg_4x14_module3/L
- U4 pad 15: unconnected-(U4-ROW10/K8-Pad15) -> /control_module/seg_4x14_module3/K
- U4 pad 16: unconnected-(U4-ROW9/K7-Pad16) -> /control_module/seg_4x14_module3/J
- U4 pad 17: unconnected-(U4-ROW8/K6-Pad17) -> /control_module/seg_4x14_module3/H
- U4 pad 18: unconnected-(U4-ROW7/K5-Pad18) -> /control_module/seg_4x14_module3/G2
- U4 pad 19: unconnected-(U4-ROW6/K4-Pad19) -> /control_module/seg_4x14_module3/G1
- U4 pad 2: unconnected-(U4-COM0/AD-Pad2) -> /control_module/seg_4x14_module3/AD
- U4 pad 20: unconnected-(U4-ROW5/K3-Pad20) -> /control_module/seg_4x14_module3/F
- U4 pad 21: unconnected-(U4-ROW4/K2-Pad21) -> /control_module/seg_4x14_module3/E
- U4 pad 22: unconnected-(U4-ROW3/K1-Pad22) -> /control_module/seg_4x14_module3/D
- U4 pad 23: unconnected-(U4-ROW2/A0-Pad23) -> /control_module/seg_4x14_module3/A0
- U4 pad 24: unconnected-(U4-ROW1/A1-Pad24) -> /control_module/seg_4x14_module3/A1
- U4 pad 25: unconnected-(U4-ROW0/A2-Pad25) -> /control_module/seg_4x14_module3/A
- U4 pad 3: unconnected-(U4-COM1/KS0-Pad3) -> /control_module/seg_4x14_module3/COM1
- U4 pad 4: unconnected-(U4-COM2/KS1-Pad4) -> /control_module/seg_4x14_module3/COM2
- U4 pad 5: unconnected-(U4-COM3/KS2-Pad5) -> /control_module/seg_4x14_module3/COM3
- U5 pad 11: unconnected-(U5-ROW14/K12-Pad11) -> /control_module/seg_4x14_module4/DP
- U5 pad 12: unconnected-(U5-ROW13/K11-Pad12) -> /control_module/seg_4x14_module4/N
- U5 pad 13: unconnected-(U5-ROW12/K10-Pad13) -> /control_module/seg_4x14_module4/M
- U5 pad 14: unconnected-(U5-ROW11/K9-Pad14) -> /control_module/seg_4x14_module4/L
- U5 pad 15: unconnected-(U5-ROW10/K8-Pad15) -> /control_module/seg_4x14_module4/K
- U5 pad 16: unconnected-(U5-ROW9/K7-Pad16) -> /control_module/seg_4x14_module4/J
- U5 pad 17: unconnected-(U5-ROW8/K6-Pad17) -> /control_module/seg_4x14_module4/H
- U5 pad 18: unconnected-(U5-ROW7/K5-Pad18) -> /control_module/seg_4x14_module4/G2
- U5 pad 19: unconnected-(U5-ROW6/K4-Pad19) -> /control_module/seg_4x14_module4/G1
- U5 pad 2: unconnected-(U5-COM0/AD-Pad2) -> /control_module/seg_4x14_module4/AD
- U5 pad 20: unconnected-(U5-ROW5/K3-Pad20) -> /control_module/seg_4x14_module4/F
- U5 pad 21: unconnected-(U5-ROW4/K2-Pad21) -> /control_module/seg_4x14_module4/E
- U5 pad 22: unconnected-(U5-ROW3/K1-Pad22) -> /control_module/seg_4x14_module4/D
- U5 pad 23: unconnected-(U5-ROW2/A0-Pad23) -> /control_module/seg_4x14_module4/A0
- U5 pad 24: unconnected-(U5-ROW1/A1-Pad24) -> /control_module/seg_4x14_module4/A1
- U5 pad 25: unconnected-(U5-ROW0/A2-Pad25) -> /control_module/seg_4x14_module4/A
- U5 pad 3: unconnected-(U5-COM1/KS0-Pad3) -> /control_module/seg_4x14_module4/COM1
- U5 pad 4: unconnected-(U5-COM2/KS1-Pad4) -> /control_module/seg_4x14_module4/COM2
- U5 pad 5: unconnected-(U5-COM3/KS2-Pad5) -> /control_module/seg_4x14_module4/COM3
- U6 pad 11: unconnected-(U6-ROW14/K12-Pad11) -> /control_module/seg_4x14_module5/DP
- U6 pad 12: unconnected-(U6-ROW13/K11-Pad12) -> /control_module/seg_4x14_module5/N
- U6 pad 13: unconnected-(U6-ROW12/K10-Pad13) -> /control_module/seg_4x14_module5/M
- U6 pad 14: unconnected-(U6-ROW11/K9-Pad14) -> /control_module/seg_4x14_module5/L
- U6 pad 15: unconnected-(U6-ROW10/K8-Pad15) -> /control_module/seg_4x14_module5/K
- U6 pad 16: unconnected-(U6-ROW9/K7-Pad16) -> /control_module/seg_4x14_module5/J
- U6 pad 17: unconnected-(U6-ROW8/K6-Pad17) -> /control_module/seg_4x14_module5/H
- U6 pad 18: unconnected-(U6-ROW7/K5-Pad18) -> /control_module/seg_4x14_module5/G2
- U6 pad 19: unconnected-(U6-ROW6/K4-Pad19) -> /control_module/seg_4x14_module5/G1
- U6 pad 2: unconnected-(U6-COM0/AD-Pad2) -> /control_module/seg_4x14_module5/AD
- U6 pad 20: unconnected-(U6-ROW5/K3-Pad20) -> /control_module/seg_4x14_module5/F
- U6 pad 21: unconnected-(U6-ROW4/K2-Pad21) -> /control_module/seg_4x14_module5/E
- U6 pad 22: unconnected-(U6-ROW3/K1-Pad22) -> /control_module/seg_4x14_module5/D
- U6 pad 23: unconnected-(U6-ROW2/A0-Pad23) -> /control_module/seg_4x14_module5/A0
- U6 pad 24: unconnected-(U6-ROW1/A1-Pad24) -> /control_module/seg_4x14_module5/A1
- U6 pad 25: unconnected-(U6-ROW0/A2-Pad25) -> /control_module/seg_4x14_module5/A
- U6 pad 3: unconnected-(U6-COM1/KS0-Pad3) -> /control_module/seg_4x14_module5/COM1
- U6 pad 4: unconnected-(U6-COM2/KS1-Pad4) -> /control_module/seg_4x14_module5/COM2
- U6 pad 5: unconnected-(U6-COM3/KS2-Pad5) -> /control_module/seg_4x14_module5/COM3
